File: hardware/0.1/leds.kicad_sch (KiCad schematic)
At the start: 16 parts, among them Q2 BSS138, Q3 BSS138, Q4 BSS138

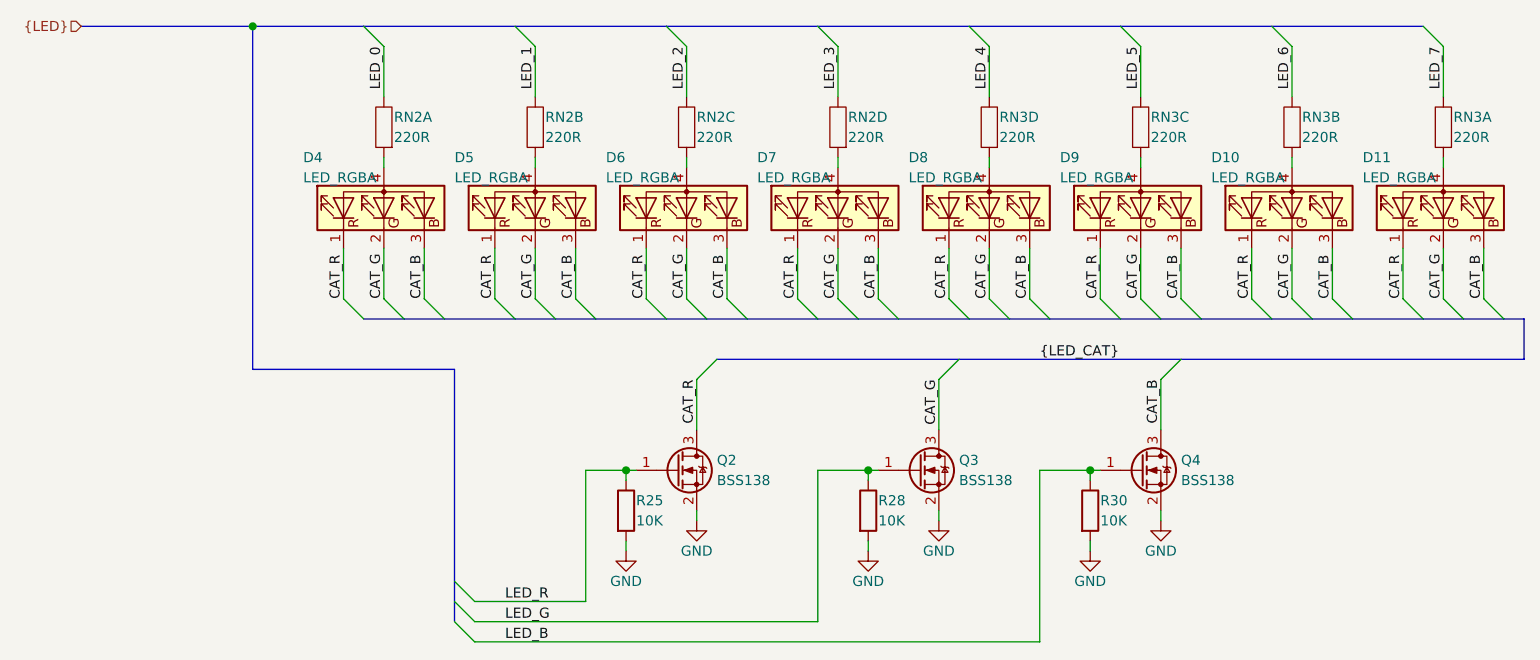
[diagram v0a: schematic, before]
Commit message: change LEDs, optimise parts
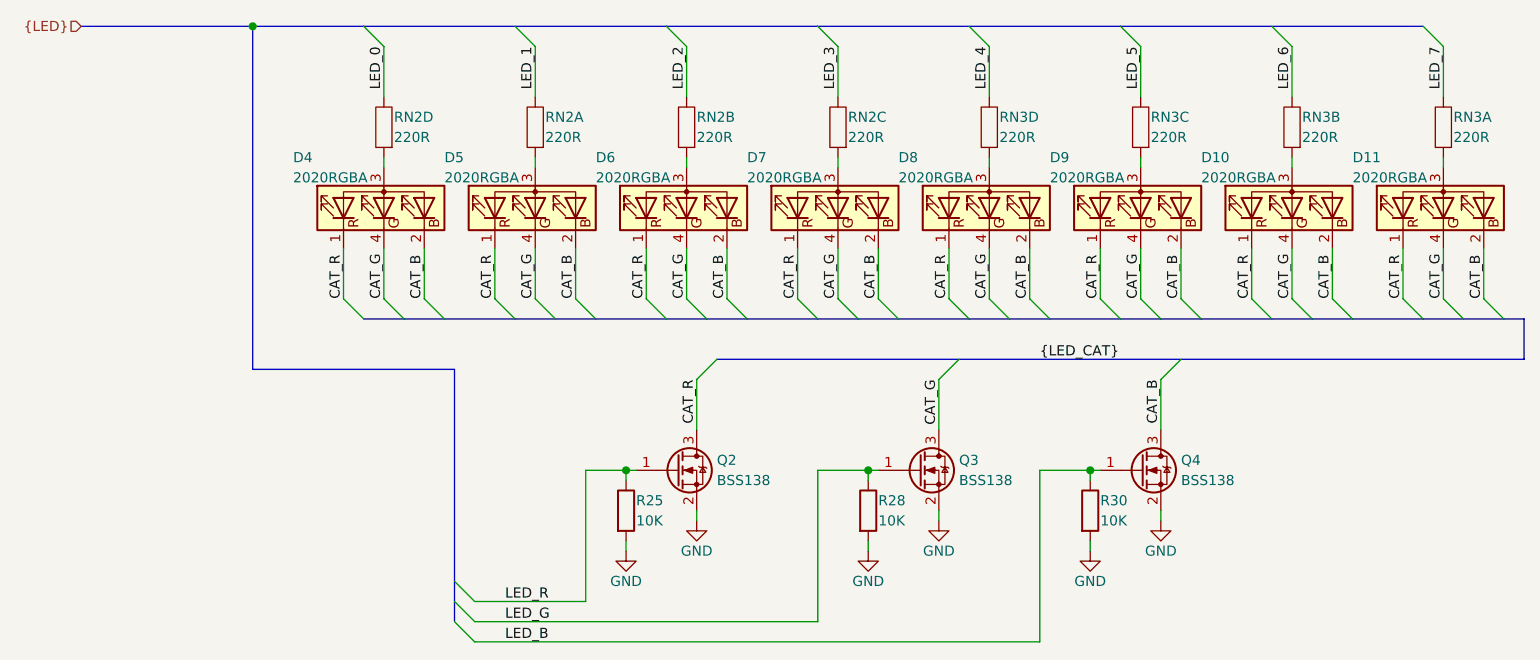
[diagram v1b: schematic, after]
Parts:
- removed D10, D11, D4, D5, D6, D7, D8, D9: LED_RGBA, josh-led:LED_0606_E6C0606RGBC3UDA, symbol josh-led:LED_RGBA
- added D10, D11, D4, D5, D6, D7, D8, D9: 2020RGBA, josh-led:LED_TRI_2020, symbol Device:LED_RBAG
- Q2, Q3, Q4: LCSC (none) -> C193366; MPN (none) -> BSS138PW,115
- RN2, RN3: LCSC (none) -> C25498; MPN (none) -> 4D02WGJ0221TCE
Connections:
- net CAT_B: now also D10.2 (BK), D11.2 (BK), D4.2 (BK), D5.2 (BK), D6.2 (BK), D7.2 (BK), D8.2 (BK), D9.2 (BK)
- net CAT_G: now also D10.4 (GK), D11.4 (GK), D4.4 (GK), D5.4 (GK), D6.4 (GK), D7.4 (GK), D8.4 (GK), D9.4 (GK)
- net CAT_R: now also D10.1 (RK), D11.1 (RK), D4.1 (RK), D5.1 (RK), D6.1 (RK), D7.1 (RK), D8.1 (RK), D9.1 (RK)
- net LED_0: now also RN2.8; no longer RN2.5
- net LED_1: now also RN2.5; no longer RN2.6
- net LED_2: now also RN2.6; no longer RN2.7
- net LED_3: now also RN2.7; no longer RN2.8
- net at RN2.3: now also D6.3 (A)
- net at RN2.2: now also D7.3 (A)
- net at RN2.4: now also D5.3 (A)
- net at RN3.3: now also D10.3 (A)
- net at RN3.1: now also D8.3 (A)
- net at RN3.2: now also D9.3 (A)
- net at RN2.1: now also D4.3 (A)
- net at RN3.4: now also D11.3 (A)
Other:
- moved on the sheet: RN2A, RN2B, RN2C, RN2D

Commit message: add part numbers
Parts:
- D10, D11, D4, D5, D6, D7, D8, D9: LCSC (none) -> C108793; Manufacturer (none) -> Foshan NationStar Optoelectronics
- Q2, Q3, Q4: Manufacturer (none) -> Nexperia
- R25, R28, R30: LCSC (none) -> C25531; MPN (none) -> 0402WGJ0103TCE; Manufacturer (none) -> UNI-ROYAL(Uniroyal Elec)
- RN2, RN3: Manufacturer (none) -> UNI-ROYAL(Uniroyal Elec)
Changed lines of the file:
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@@
+      (effects (font (size 1.27 1.27)) hide)
+    )
+    (property "Manufacturer" "UNI-ROYAL(Uniroyal Elec)" (id 4) (at 92.71 82.55 0)
       (effects (font (size 1.27 1.27)) hide)
     )
@@
       (effects (font (size 1.27 1.27)) hide)
     )
+    (property "Manufacturer" "UNI-ROYAL(Uniroyal Elec)" (id 4) (at 111.76 82.55 0)
+      (effects (font (size 1.27 1.27)) hide)
+    )
   )
   (symbol (lib_id "josh-passive:RN") (at 130.81 82.55 90) (unit 2)
@@
       (effects (font (size 1.27 1.27)) hide)
     )
+    (property "Manufacturer" "UNI-ROYAL(Uniroyal Elec)" (id 4) (at 130.81 82.55 0)
+      (effects (font (size 1.27 1.27)) hide)
+    )
   )
   (symbol (lib_id "josh-passive:RN") (at 149.86 82.55 90) (unit 3)
@@
       (effects (font (size 1.27 1.27)) hide)
     )
+    (property "Manufacturer" "UNI-ROYAL(Uniroyal Elec)" (id 4) (at 149.86 82.55 0)
+      (effects (font (size 1.27 1.27)) hide)
+    )
   )
   (symbol (lib_id "josh-passive:RN") (at 168.91 82.55 90) (unit 4)
@@
       (effects (font (size 1.27 1.27)) hide)
     )
+    (property "Manufacturer" "UNI-ROYAL(Uniroyal Elec)" (id 4) (at 168.91 82.55 0)
+      (effects (font (size 1.27 1.27)) hide)
+    )
   )
   (symbol (lib_id "josh-passive:RN") (at 187.96 82.55 90) (unit 3)
@@
       (effects (font (size 1.27 1.27)) hide)
     )
+    (property "Manufacturer" "UNI-ROYAL(Uniroyal Elec)" (id 4) (at 187.96 82.55 0)
+      (effects (font (size 1.27 1.27)) hide)
+    )
   )
   (symbol (lib_id "josh-passive:RN") (at 207.01 82.55 90) (unit 2)
@@
       (effects (font (size 1.27 1.27)) hide)
     )
+    (property "Manufacturer" "UNI-ROYAL(Uniroyal Elec)" (id 4) (at 207.01 82.55 0)
+      (effects (font (size 1.27 1.27)) hide)
+    )
   )
   (symbol (lib_id "josh-passive:RN") (at 226.06 82.55 90) (unit 1)
@@
       (effects (font (size 1.27 1.27)) hide)
     )
+    (property "Manufacturer" "UNI-ROYAL(Uniroyal Elec)" (id 4) (at 226.06 82.55 0)
+      (effects (font (size 1.27 1.27)) hide)
+    )
   )
   (symbol (lib_id "Device:R") (at 123.19 130.81 0) (unit 1)
@@
       (effects (font (size 1.27 1.27)) hide)
     )
+    (property "LCSC" "C25531" (id 4) (at 123.19 130.81 0)
+      (effects (font (size 1.27 1.27)) hide)
+    )
+    (property "MPN" "0402WGJ0103TCE" (id 5) (at 123.19 130.81 0)
+      (effects (font (size 1.27 1.27)) hide)
+    )
+    (property "Manufacturer" "UNI-ROYAL(Uniroyal Elec)" (id 6) (at 123.19 130.81 0)
+      (effects (font (size 1.27 1.27)) hide)
+    )
   )
   (symbol (lib_id "Device:R") (at 153.67 130.81 0) (unit 1)
@@
       (effects (font (size 1.27 1.27)) hide)
     )
+    (property "LCSC" "C25531" (id 4) (at 153.67 130.81 0)
+      (effects (font (size 1.27 1.27)) hide)
+    )
+    (property "MPN" "0402WGJ0103TCE" (id 5) (at 153.67 130.81 0)
+      (effects (font (size 1.27 1.27)) hide)
+    )
+    (property "Manufacturer" "UNI-ROYAL(Uniroyal Elec)" (id 6) (at 153.67 130.81 0)
+      (effects (font (size 1.27 1.27)) hide)
+    )
   )
   (symbol (lib_id "Device:R") (at 181.61 130.81 0) (unit 1)
@@
     )
     (property "Datasheet" "~" (id 3) (at 181.61 130.81 0)
+      (effects (font (size 1.27 1.27)) hide)
+    )
+    (property "LCSC" "C25531" (id 4) (at 181.61 130.81 0)
+      (effects (font (size 1.27 1.27)) hide)
+    )
+    (property "MPN" "0402WGJ0103TCE" (id 5) (at 181.61 130.81 0)
+      (effects (font (size 1.27 1.27)) hide)
+    )
+    (property "Manufacturer" "UNI-ROYAL(Uniroyal Elec)" (id 6) (at 181.61 130.81 0)
       (effects (font (size 1.27 1.27)) hide)
     )
@@
       (effects (font (size 1.27 1.27)) hide)
     )
+    (property "Manufacturer" "Nexperia" (id 4) (at 129.54 125.73 0)
+      (effects (font (size 1.27 1.27)) hide)
+    )
   )
   (symbol (lib_id "Transistor_FET:BSS138") (at 160.02 125.73 0) (unit 1)
@@
       (effects (font (size 1.27 1.27)) hide)
     )
+    (property "Manufacturer" "Nexperia" (id 4) (at 160.02 125.73 0)
+      (effects (font (size 1.27 1.27)) hide)
+    )
   )
   (symbol (lib_id "Transistor_FET:BSS138") (at 187.96 125.73 0) (unit 1)
@@
       (effects (font (size 1.27 1.27)) hide)
     )
+    (property "Manufacturer" "Nexperia" (id 4) (at 187.96 125.73 0)
+      (effects (font (size 1.27 1.27)) hide)
+    )
   )
   (symbol (lib_id "Device:LED_RBAG") (at 92.71 92.71 90) (unit 1)
@@
       (effects (font (size 1.27 1.27)) hide)
     )
+    (property "LCSC" "C108793" (id 4) (at 92.71 92.71 0)
+      (effects (font (size 1.27 1.27)) hide)
+    )
+    (property "Manufacturer" "Foshan NationStar Optoelectronics" (id 5) (at 92.71 92.71 0)
+      (effects (font (size 1.27 1.27)) hide)
+    )
   )
   (symbol (lib_id "Device:LED_RBAG") (at 111.76 92.71 90) (unit 1)
@@
       (effects (font (size 1.27 1.27)) hide)
     )
+    (property "LCSC" "C108793" (id 4) (at 111.76 92.71 0)
+      (effects (font (size 1.27 1.27)) hide)
+    )
+    (property "Manufacturer" "Foshan NationStar Optoelectronics" (id 5) (at 111.76 92.71 0)
+      (effects (font (size 1.27 1.27)) hide)
+    )
   )
   (symbol (lib_id "Device:LED_RBAG") (at 130.81 92.71 90) (unit 1)
@@
       (effects (font (size 1.27 1.27)) hide)
     )
+    (property "LCSC" "C108793" (id 4) (at 130.81 92.71 0)
+      (effects (font (size 1.27 1.27)) hide)
+    )
+    (property "Manufacturer" "Foshan NationStar Optoelectronics" (id 5) (at 130.81 92.71 0)
+      (effects (font (size 1.27 1.27)) hide)
+    )
   )
   (symbol (lib_id "Device:LED_RBAG") (at 149.86 92.71 90) (unit 1)
@@
       (effects (font (size 1.27 1.27)) hide)
     )
+    (property "LCSC" "C108793" (id 4) (at 149.86 92.71 0)
+      (effects (font (size 1.27 1.27)) hide)
+    )
+    (property "Manufacturer" "Foshan NationStar Optoelectronics" (id 5) (at 149.86 92.71 0)
+      (effects (font (size 1.27 1.27)) hide)
+    )
   )
   (symbol (lib_id "Device:LED_RBAG") (at 168.91 92.71 90) (unit 1)
@@
       (effects (font (size 1.27 1.27)) hide)
     )
+    (property "LCSC" "C108793" (id 4) (at 168.91 92.71 0)
+      (effects (font (size 1.27 1.27)) hide)
+    )
+    (property "Manufacturer" "Foshan NationStar Optoelectronics" (id 5) (at 168.91 92.71 0)
+      (effects (font (size 1.27 1.27)) hide)
+    )
   )
   (symbol (lib_id "Device:LED_RBAG") (at 187.96 92.71 90) (unit 1)
@@
       (effects (font (size 1.27 1.27)) hide)
     )
+    (property "LCSC" "C108793" (id 4) (at 187.96 92.71 0)
+      (effects (font (size 1.27 1.27)) hide)
+    )
+    (property "Manufacturer" "Foshan NationStar Optoelectronics" (id 5) (at 187.96 92.71 0)
+      (effects (font (size 1.27 1.27)) hide)
+    )
   )
   (symbol (lib_id "Device:LED_RBAG") (at 207.01 92.71 90) (unit 1)
@@
       (effects (font (size 1.27 1.27)) hide)
     )
+    (property "LCSC" "C108793" (id 4) (at 207.01 92.71 0)
+      (effects (font (size 1.27 1.27)) hide)
+    )
+    (property "Manufacturer" "Foshan NationStar Optoelectronics" (id 5) (at 207.01 92.71 0)
+      (effects (font (size 1.27 1.27)) hide)
+    )
   )
   (symbol (lib_id "Device:LED_RBAG") (at 226.06 92.71 90) (unit 1)
@@
       (effects (font (size 1.27 1.27)) hide)
     )
+    (property "LCSC" "C108793" (id 4) (at 226.06 92.71 0)
+      (effects (font (size 1.27 1.27)) hide)
+    )
+    (property "Manufacturer" "Foshan NationStar Optoelectronics" (id 5) (at 226.06 92.71 0)
+      (effects (font (size 1.27 1.27)) hide)
+    )

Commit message: design review done
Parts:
- D10, D11, D4, D5, D6, D7, D8, D9: LCSC C108793 -> (none)
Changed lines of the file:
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@@
-      (effects (font (size 1.27 1.27)) hide)
-    )
-    (property "LCSC" "C108793" (id 4) (at 92.71 92.71 0)
       (effects (font (size 1.27 1.27)) hide)
     )
@@
       (effects (font (size 1.27 1.27)) hide)
     )
-    (property "LCSC" "C108793" (id 4) (at 111.76 92.71 0)
-      (effects (font (size 1.27 1.27)) hide)
-    )
     (property "Manufacturer" "Foshan NationStar Optoelectronics" (id 5) (at 111.76 92.71 0)
       (effects (font (size 1.27 1.27)) hide)
@@
     )
     (property "MPN" "FM-B2020RGBA-HG" (id 4) (at 130.81 92.71 90)
-      (effects (font (size 1.27 1.27)) hide)
-    )
-    (property "LCSC" "C108793" (id 4) (at 130.81 92.71 0)
       (effects (font (size 1.27 1.27)) hide)
     )
@@
       (effects (font (size 1.27 1.27)) hide)
     )
-    (property "LCSC" "C108793" (id 4) (at 149.86 92.71 0)
-      (effects (font (size 1.27 1.27)) hide)
-    )
     (property "Manufacturer" "Foshan NationStar Optoelectronics" (id 5) (at 149.86 92.71 0)
       (effects (font (size 1.27 1.27)) hide)
@@
     )
     (property "MPN" "FM-B2020RGBA-HG" (id 4) (at 168.91 92.71 90)
-      (effects (font (size 1.27 1.27)) hide)
-    )
-    (property "LCSC" "C108793" (id 4) (at 168.91 92.71 0)
       (effects (font (size 1.27 1.27)) hide)
     )
@@
       (effects (font (size 1.27 1.27)) hide)
     )
-    (property "LCSC" "C108793" (id 4) (at 187.96 92.71 0)
-      (effects (font (size 1.27 1.27)) hide)
-    )
     (property "Manufacturer" "Foshan NationStar Optoelectronics" (id 5) (at 187.96 92.71 0)
       (effects (font (size 1.27 1.27)) hide)
@@
     )
     (property "MPN" "FM-B2020RGBA-HG" (id 4) (at 207.01 92.71 90)
-      (effects (font (size 1.27 1.27)) hide)
-    )
-    (property "LCSC" "C108793" (id 4) (at 207.01 92.71 0)
       (effects (font (size 1.27 1.27)) hide)
     )
@@
       (effects (font (size 1.27 1.27)) hide)
     )
-    (property "LCSC" "C108793" (id 4) (at 226.06 92.71 0)
-      (effects (font (size 1.27 1.27)) hide)
-    )

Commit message: update BOM
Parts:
- D10, D11, D4, D5, D6, D7, D8, D9: LCSC (none) -> C108793
- Q2, Q3, Q4: Mouser (none) -> 771-BSS138PW115
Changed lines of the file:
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@@
-(kicad_sch (version 20200828) (generator eeschema)
-  (page 2 5)
+(kicad_sch (version 20201015) (generator eeschema)
+  (page 1 5)
   (paper "A4")
   (bus_alias "LED_CAT" (members "CAT_R" "CAT_G" "CAT_B"))
@@
       (effects (font (size 1.27 1.27)) hide)
     )
+    (property "Mouser" "771-BSS138PW115 " (id 4) (at 129.54 125.73 0)
+      (effects (font (size 1.27 1.27)) hide)
+    )
   )
   (symbol (lib_id "Transistor_FET:BSS138") (at 160.02 125.73 0) (unit 1)
@@
       (effects (font (size 1.27 1.27)) hide)
     )
+    (property "Mouser" "771-BSS138PW115 " (id 4) (at 160.02 125.73 0)
+      (effects (font (size 1.27 1.27)) hide)
+    )
   )
   (symbol (lib_id "Transistor_FET:BSS138") (at 187.96 125.73 0) (unit 1)
@@
       (effects (font (size 1.27 1.27)) hide)
     )
+    (property "Mouser" "771-BSS138PW115 " (id 4) (at 187.96 125.73 0)
+      (effects (font (size 1.27 1.27)) hide)
+    )
   )
   (symbol (lib_id "Device:LED_RBAG") (at 92.71 92.71 90) (unit 1)
@@
       (effects (font (size 1.27 1.27)) hide)
     )
+    (property "LCSC" "C108793" (id 4) (at 92.71 92.71 0)
+      (effects (font (size 1.27 1.27)) hide)
+    )
   )
   (symbol (lib_id "Device:LED_RBAG") (at 111.76 92.71 90) (unit 1)
@@
       (effects (font (size 1.27 1.27)) hide)
     )
+    (property "LCSC" "C108793" (id 4) (at 111.76 92.71 0)
+      (effects (font (size 1.27 1.27)) hide)
+    )
   )
   (symbol (lib_id "Device:LED_RBAG") (at 130.81 92.71 90) (unit 1)
@@
       (effects (font (size 1.27 1.27)) hide)
     )
+    (property "LCSC" "C108793" (id 4) (at 130.81 92.71 0)
+      (effects (font (size 1.27 1.27)) hide)
+    )
   )
   (symbol (lib_id "Device:LED_RBAG") (at 149.86 92.71 90) (unit 1)
@@
       (effects (font (size 1.27 1.27)) hide)
     )
+    (property "LCSC" "C108793" (id 4) (at 149.86 92.71 0)
+      (effects (font (size 1.27 1.27)) hide)
+    )
   )
   (symbol (lib_id "Device:LED_RBAG") (at 168.91 92.71 90) (unit 1)
@@
       (effects (font (size 1.27 1.27)) hide)
     )
+    (property "LCSC" "C108793" (id 4) (at 168.91 92.71 0)
+      (effects (font (size 1.27 1.27)) hide)
+    )
   )
   (symbol (lib_id "Device:LED_RBAG") (at 187.96 92.71 90) (unit 1)
@@
       (effects (font (size 1.27 1.27)) hide)
     )
+    (property "LCSC" "C108793" (id 4) (at 187.96 92.71 0)
+      (effects (font (size 1.27 1.27)) hide)
+    )
   )
   (symbol (lib_id "Device:LED_RBAG") (at 207.01 92.71 90) (unit 1)
@@
       (effects (font (size 1.27 1.27)) hide)
     )
+    (property "LCSC" "C108793" (id 4) (at 207.01 92.71 0)
+      (effects (font (size 1.27 1.27)) hide)
+    )
   )
   (symbol (lib_id "Device:LED_RBAG") (at 226.06 92.71 90) (unit 1)
@@
       (effects (font (size 1.27 1.27)) hide)
     )
+    (property "LCSC" "C108793" (id 4) (at 226.06 92.71 0)
+      (effects (font (size 1.27 1.27)) hide)
+    )
